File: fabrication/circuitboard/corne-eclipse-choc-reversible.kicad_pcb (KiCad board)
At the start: 4 copper layers, 150.6 x 105.7 mm, 91 parts, among them J2 OLED, SW1 SW_Choc_v1v2_HS, SW10 SW_Choc_v1v2_HS, SW11 SW_Choc_v1v2_HS, SW12 SW_Choc_v1v2_HS, SW13 SW_Choc_v1v2_HS, SW14 SW_Choc_v1v2_HS, SW15 SW_Choc_v1v2_HS, SW16 SW_Choc_v1v2_HS, SW17 SW_Choc_v1v2_HS, SW18 SW_Choc_v1v2_HS, SW2 SW_Choc_v1v2_HS, SW20 SW_Choc_v1v2_HS, SW21 SW_Choc_v1v2_HS, SW22 SW_Choc_v1v2_HS, SW3 SW_Choc_v1v2_HS, SW4 SW_Choc_v1v2_HS, SW5 SW_Choc_v1v2_HS, SW6 SW_Choc_v1v2_HS, SW7 SW_Choc_v1v2_HS, SW8 SW_Choc_v1v2_HS, SW9 SW_Choc_v1v2_HS, U1 nice!nano

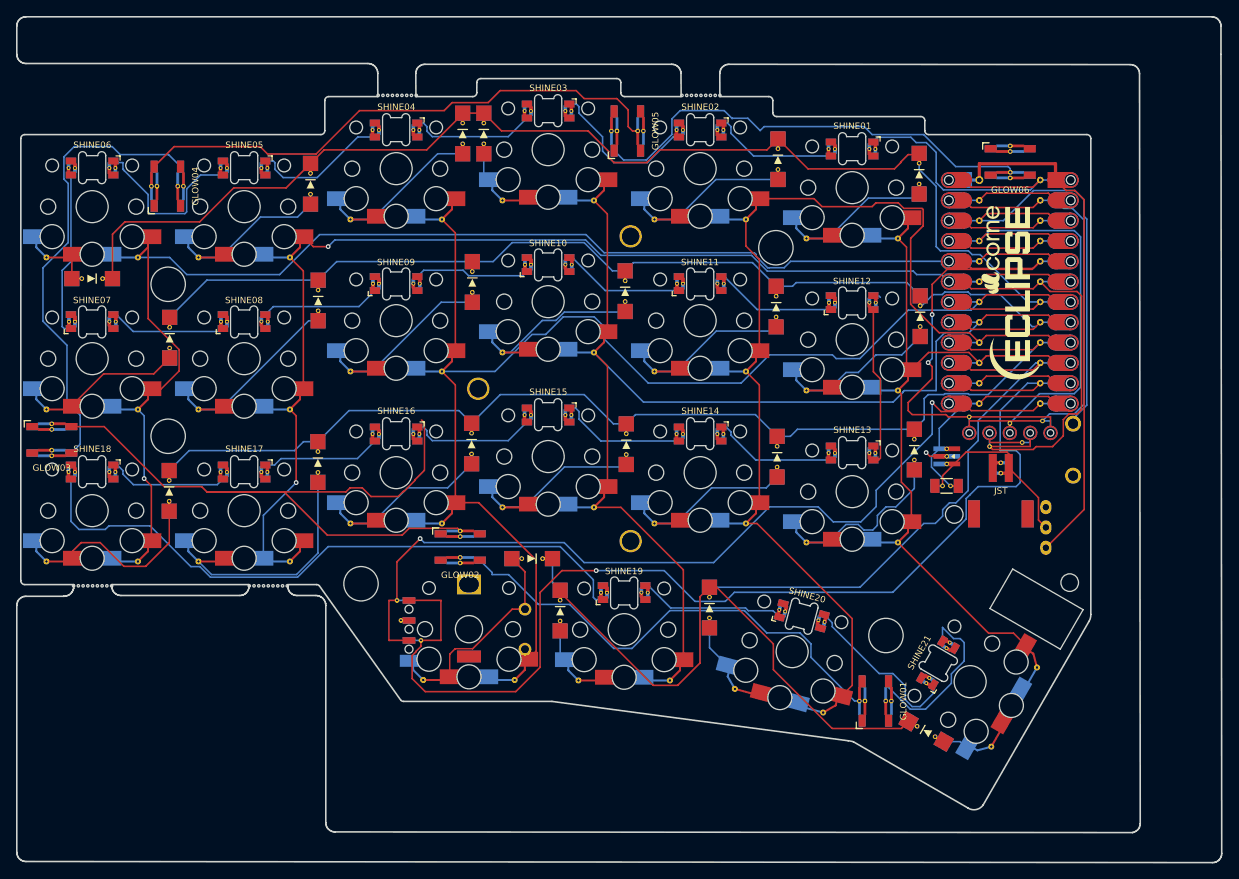
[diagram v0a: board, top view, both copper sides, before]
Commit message: wip(pcbs): reversible encoder polarity + fab cleanup
Encoder footprints now flip A/B labels per side so the body-on-back
mount (encoder rotated 180°) lands on the correct nets. Niceview safe
zones, BT mouse-bite repitch, mask-bridge cleanup, and JLCPCB-friendly
drill/track minimums.

Co-Authored-By: Claude Opus 4.6 (1M context) <noreply@anthropic.com>
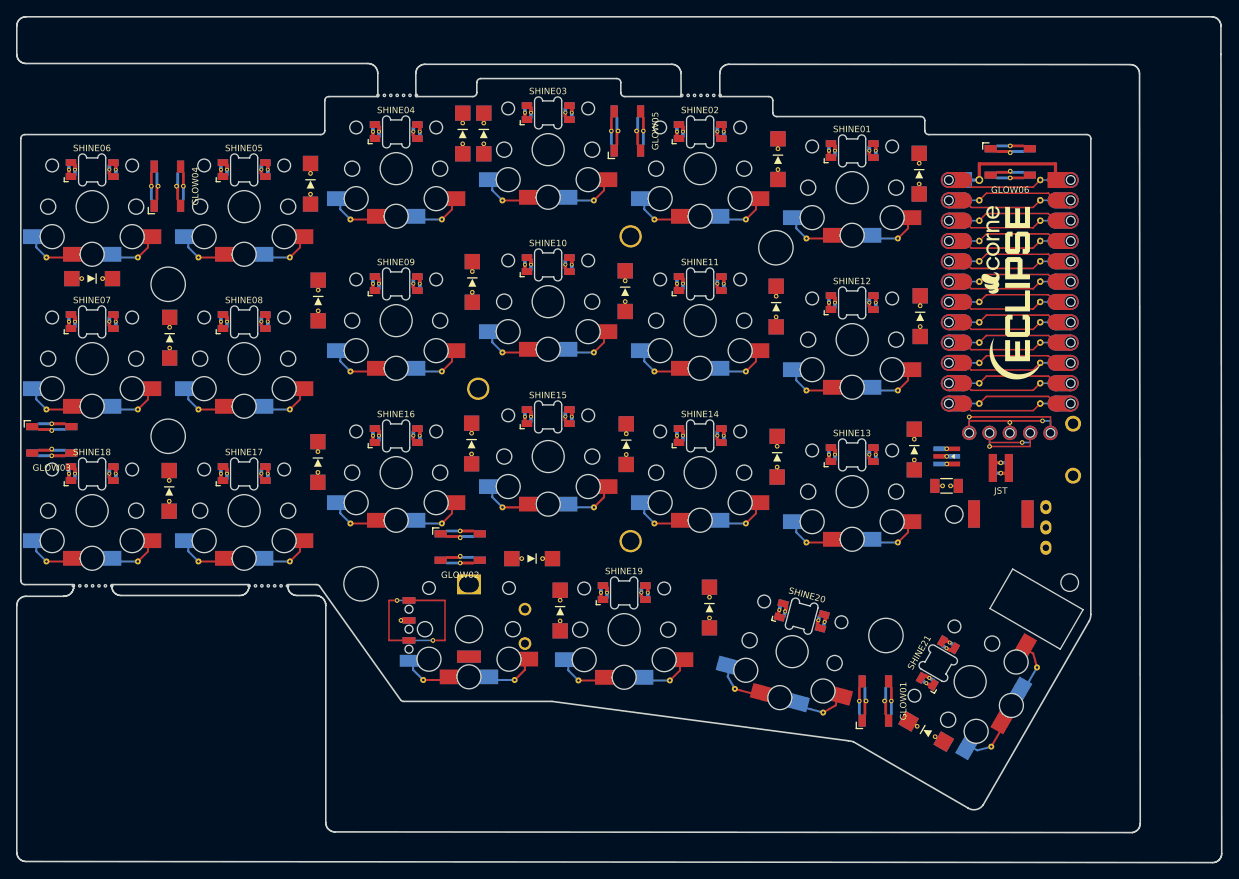
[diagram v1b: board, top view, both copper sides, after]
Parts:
- turned SHINE01 to 180 degrees
- turned SHINE02 to 180 degrees
- turned SHINE03 to 180 degrees
- turned SHINE04 to 180 degrees
- turned SHINE05 to 180 degrees
- turned SHINE06 to 180 degrees
- turned SHINE13 to 180 degrees
- turned SHINE14 to 180 degrees
- turned SHINE15 to 180 degrees
- turned SHINE16 to 180 degrees
- turned SHINE17 to 180 degrees
- turned SHINE18 to 180 degrees
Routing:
- net col0: track 151.5 -> 0.00 mm, vias 1 -> 0
- net row0: track 147.7 -> 0.00 mm
- net col2: track 139.0 -> 0.00 mm
- net row3: track 130.3 -> 0.00 mm
- net col1: track 125.7 -> 0.00 mm, vias 2 -> 0
- net row2: track 123.7 -> 0.00 mm
- net Net-(U1-Pad11): track 120.5 -> 0.00 mm, vias 1 -> 0
- net row1: track 120.2 -> 0.00 mm
- net col3: track 118.8 -> 0.00 mm
- net col4: track 107.1 -> 0.00 mm
- net Net-(U1-Pad12): track 92.4 -> 0.00 mm, vias 2 -> 0
- net led24-led25: track 90.4 -> 0.00 mm
- net led18-led19: track 80.7 -> 0.00 mm
- net led26-led27: track 68.5 -> 0.00 mm
- net col5: track 65.4 -> 0.00 mm
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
